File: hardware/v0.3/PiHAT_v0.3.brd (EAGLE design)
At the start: 65 x 56.5 mm, 37 parts, among them IC1 BMP280, J1 FTDI, J3 ISP, U1 ATMEGA328P, U2 TSL2561, U3 OPA344, U6 ADMP401, U7 SHT31/35, U8 CCS811, Y1 16MHZ

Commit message: Some trace adjustments
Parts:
- moved C12 6.73 mm to (10.9, 19.6)
- moved LED2 0.97 mm to (47.2, 46.2)
- moved R10 0.97 mm to (45.4, 46.1)
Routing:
- net DTR: track 8.87 -> 3.26 mm
- net RESET: track 67.8 -> 65.8 mm

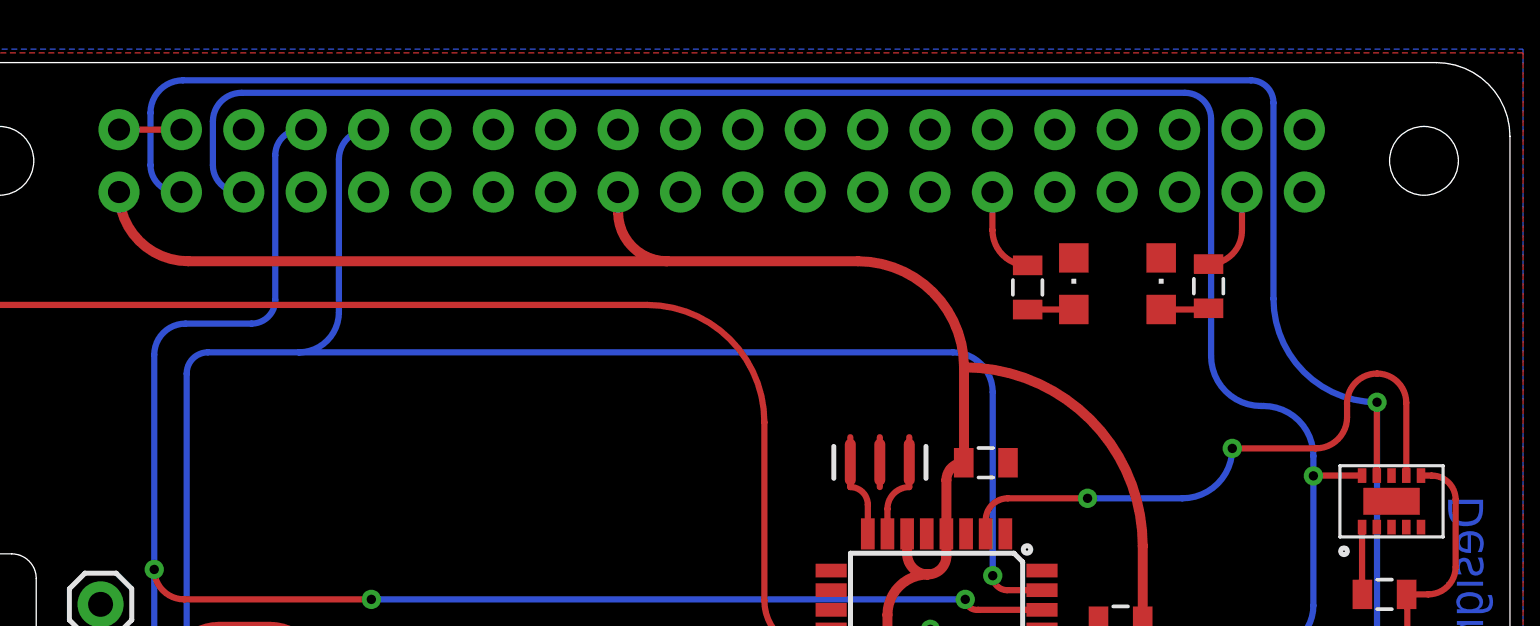
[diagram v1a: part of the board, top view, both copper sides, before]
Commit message: Added jumpers on the I2C line
Jumpers between Pi's SDA and SCL lines and ATmega's SDA and SCL lines
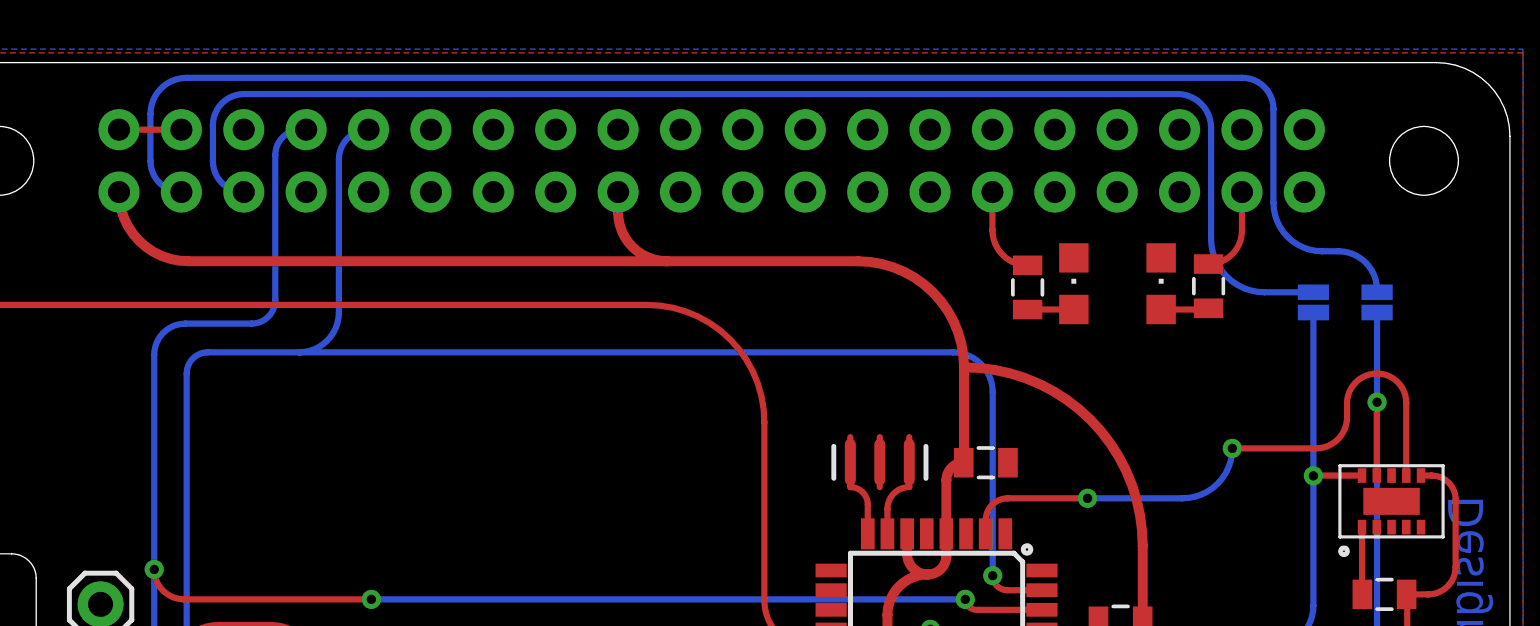
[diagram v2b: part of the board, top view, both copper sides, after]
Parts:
- added JP1: SDA, SparkFun-Passives:PAD-JUMPER-2-NC_BY_PASTE_YES_SILK_FULL_BOX
- added JP2: SCL, SparkFun-Passives:PAD-JUMPER-2-NC_BY_PASTE_YES_SILK_FULL_BOX
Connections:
- new net PI_SCL: JP2.2, RPI1.5
- new net PI_SDA: JP1.2, RPI1.3
- net SCL: now also JP2.1; no longer RPI1.5
- net SDA: now also JP1.1; no longer RPI1.3
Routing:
- net SDA: track 166.4 -> 105.6 mm
- net PI_SDA: track 0.00 -> 60.1 mm
- net SCL: track 153.0 -> 98.2 mm
- net PI_SCL: track 0.00 -> 54.6 mm
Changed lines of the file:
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@@
 <attribute name="VALUE" x="39.3192" y="8.0518" size="0.8128" layer="121" font="vector" rot="R180"/>
+</element>
+<element name="JP1" library="SparkFun-Passives" package="PAD-JUMPER-2-NC_BY_PASTE_YES_SILK_FULL_BOX" value="SDA" x="59.5884" y="45.466" smashed="yes" rot="MR90">
+<attribute name="VALUE" x="61.7474" y="46.619" size="0.8128" layer="122" font="vector" rot="MR270"/>
+</element>
+<element name="JP2" library="SparkFun-Passives" package="PAD-JUMPER-2-NC_BY_PASTE_YES_SILK_FULL_BOX" value="SCL" x="56.9976" y="45.466" smashed="yes" rot="MR90">
+<attribute name="VALUE" x="55.6006" y="46.4666" size="0.8128" layer="122" font="vector" rot="SMR270"/>
 </element>
 </elements>
@@
 <wire x1="43.3832" y1="29.8704" x2="58.674" y2="29.8704" width="0.254" layer="16"/>
 <wire x1="58.674" y1="29.8704" x2="59.5884" y2="30.7848" width="0.254" layer="16" curve="90"/>
-<contactref element="RPI1" pad="3"/>
-<wire x1="10.91" y1="49.96" x2="10.746" y2="49.96" width="0.254" layer="16"/>
-<wire x1="10.746" y1="49.96" x2="9.652" y2="51.054" width="0.254" layer="16" curve="-90"/>
-<wire x1="9.652" y1="51.054" x2="9.652" y2="53.1876" width="0.254" layer="16"/>
-<wire x1="9.652" y1="53.1876" x2="10.9728" y2="54.5084" width="0.254" layer="16" curve="-90"/>
-<wire x1="10.9728" y1="54.5084" x2="54.4576" y2="54.5084" width="0.254" layer="16"/>
-<wire x1="54.4576" y1="54.5084" x2="55.372" y2="53.594" width="0.254" layer="16" curve="-90"/>
-<wire x1="55.372" y1="53.594" x2="55.372" y2="45.6184" width="0.254" layer="16"/>
-<wire x1="55.372" y1="45.6184" x2="59.5884" y2="41.402" width="0.254" layer="16" curve="90"/>
+<contactref element="JP1" pad="1"/>
+<wire x1="59.5884" y1="41.402" x2="59.5884" y2="45.0541" width="0.254" layer="16"/>
 </signal>
 <signal name="SCL">
@@
 <wire x1="55.2196" y1="31.3436" x2="56.9976" y2="33.1216" width="0.254" layer="16" curve="90"/>
 <wire x1="56.9976" y1="33.1216" x2="56.9976" y2="38.4048" width="0.254" layer="16"/>
-<contactref element="RPI1" pad="5"/>
-<wire x1="13.45" y1="49.96" x2="13.286" y2="49.96" width="0.254" layer="16"/>
-<wire x1="13.286" y1="49.96" x2="12.192" y2="51.054" width="0.254" layer="16" curve="-90"/>
-<wire x1="12.192" y1="51.054" x2="12.192" y2="52.832" width="0.254" layer="16"/>
-<wire x1="12.192" y1="52.832" x2="13.3604" y2="54.0004" width="0.254" layer="16" curve="-90"/>
-<wire x1="13.3604" y1="54.0004" x2="51.7652" y2="54.0004" width="0.254" layer="16"/>
-<wire x1="51.7652" y1="54.0004" x2="52.832" y2="52.9336" width="0.254" layer="16" curve="-90"/>
-<wire x1="52.832" y1="52.9336" x2="52.832" y2="43.2816" width="0.254" layer="16"/>
-<wire x1="56.9976" y1="38.4048" x2="56.9976" y2="39.2176" width="0.254" layer="16"/>
-<wire x1="56.9976" y1="39.2176" x2="54.9656" y2="41.2496" width="0.254" layer="16" curve="90"/>
-<wire x1="54.9656" y1="41.2496" x2="54.864" y2="41.2496" width="0.254" layer="16"/>
-<wire x1="54.864" y1="41.2496" x2="52.832" y2="43.2816" width="0.254" layer="16" curve="-90"/>
+<contactref element="JP2" pad="1"/>
+<wire x1="56.9976" y1="38.4048" x2="56.9976" y2="45.0541" width="0.254" layer="16"/>
 </signal>
 <signal name="GPIO4">
@@
 <wire x1="57.0992" y1="39.5224" x2="53.6956" y2="39.5224" width="0.254" layer="1"/>
 </signal>
+<signal name="PI_SDA">
+<contactref element="RPI1" pad="3"/>
+<contactref element="JP1" pad="2"/>
+<wire x1="59.5884" y1="45.8779" x2="59.5884" y2="45.974" width="0.254" layer="16"/>
+<wire x1="59.5884" y1="45.974" x2="58.0136" y2="47.5488" width="0.254" layer="16" curve="90"/>
+<wire x1="58.0136" y1="47.5488" x2="57.3532" y2="47.5488" width="0.254" layer="16"/>
+<wire x1="57.3532" y1="47.5488" x2="55.372" y2="49.53" width="0.254" layer="16" curve="-90"/>
+<wire x1="55.372" y1="49.53" x2="55.372" y2="53.34" width="0.254" layer="16"/>
+<wire x1="55.372" y1="53.34" x2="54.102" y2="54.61" width="0.254" layer="16" curve="90"/>
+<wire x1="54.102" y1="54.61" x2="11.1252" y2="54.61" width="0.254" layer="16"/>
+<wire x1="11.1252" y1="54.61" x2="9.652" y2="53.1368" width="0.254" layer="16" curve="90"/>
+<wire x1="9.652" y1="53.1368" x2="9.652" y2="51.218" width="0.254" layer="16"/>
+<wire x1="9.652" y1="51.218" x2="10.91" y2="49.96" width="0.254" layer="16" curve="90"/>
+</signal>
+<signal name="PI_SCL">
+<contactref element="RPI1" pad="5"/>
+<contactref element="JP2" pad="2"/>
+<wire x1="56.9976" y1="45.8779" x2="55.0109" y2="45.8779" width="0.254" layer="16"/>
+<wire x1="55.0109" y1="45.8779" x2="52.832" y2="48.0568" width="0.254" layer="16" curve="-90"/>
+<wire x1="52.832" y1="48.0568" x2="52.832" y2="52.578" width="0.254" layer="16"/>
+<wire x1="52.832" y1="52.578" x2="51.4604" y2="53.9496" width="0.254" layer="16" curve="90"/>
+<wire x1="51.4604" y1="53.9496" x2="13.462" y2="53.9496" width="0.254" layer="16"/>
+<wire x1="13.462" y1="53.9496" x2="12.192" y2="52.6796" width="0.254" layer="16" curve="90"/>
+<wire x1="12.192" y1="52.6796" x2="12.192" y2="51.218" width="0.254" layer="16"/>
+<wire x1="12.192" y1="51.218" x2="13.45" y2="49.96" width="0.254" layer="16" curve="90"/>
+</signal>
 </signals>
